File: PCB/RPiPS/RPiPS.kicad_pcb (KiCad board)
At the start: 2 copper layers, 17 parts, among them IC1 ATTINY25-P, K1 RELAI-1RT, P1 PowerIn, P2 CONN_1, P3 PiPower, Q1 NPN, SW1 SW_PUSH

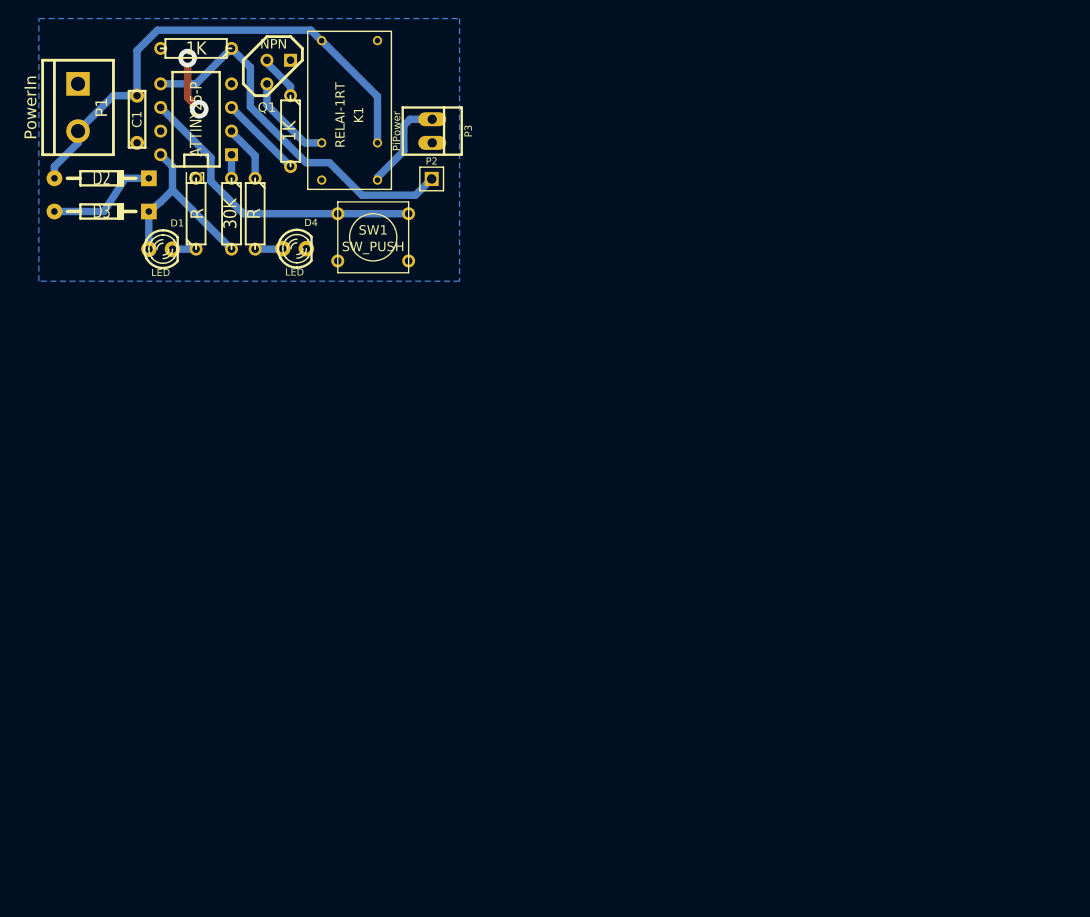
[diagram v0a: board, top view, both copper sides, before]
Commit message: Move to RPi Expansion board template
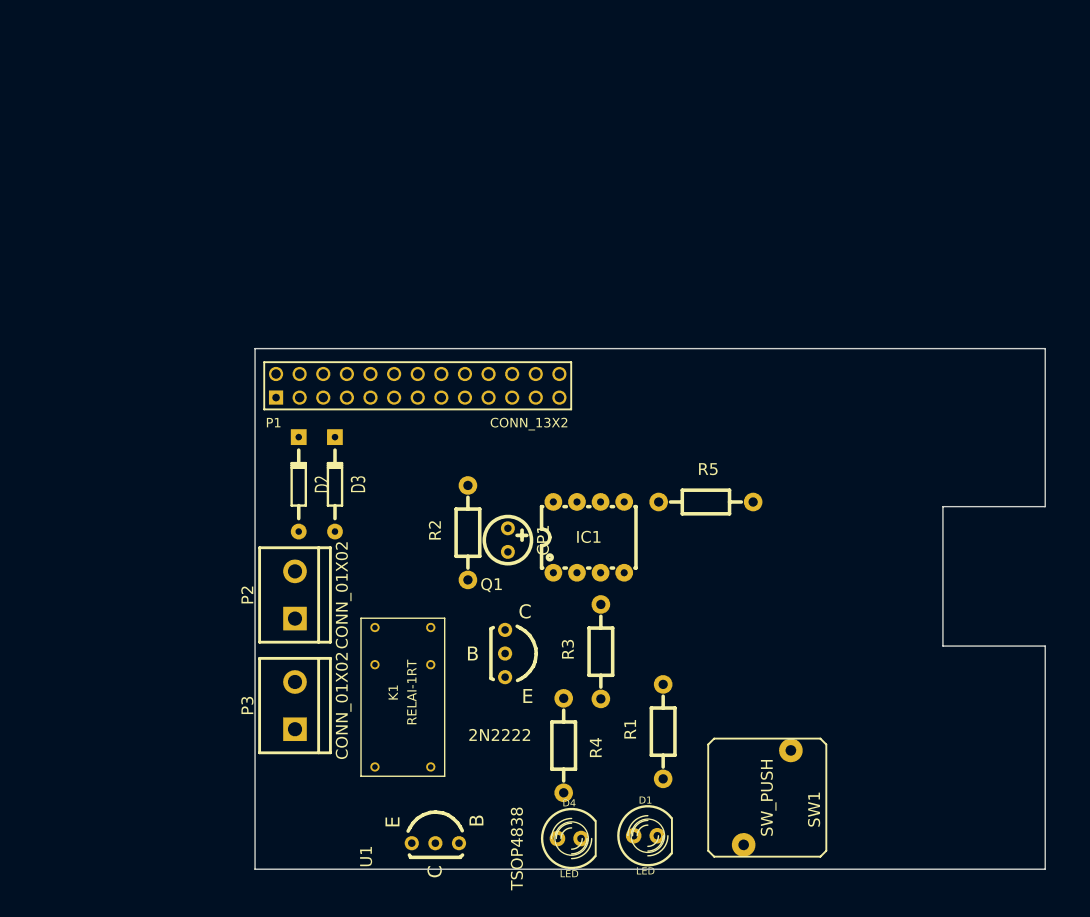
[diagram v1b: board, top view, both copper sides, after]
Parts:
- removed C1: C, Capacitors:cnp_6mm_disc
- added CP1: 100n, Capacitors_Elko_ThroughHole:Elko_vert_DM5_RM2-5, F.Cu at (170.7, 145.6)
- added U1: TSOP4838, Housings_TO-92:TO-92-Bipolar-inline-wide-ECB, F.Cu at (162.9, 178.2)
- D1, D4: footprint LEDs:LED-3MM -> LEDs:LED-5MM
- IC1: footprint Sockets_DIP:DIP-8__300 -> Power_Integrations:PDIP-8
- K1: footprint local:Relay V23040 -> relay:Relay V23040
- P1: value PowerIn -> CONN_13X2; footprint Connect:bornier2 -> pin_array_13x2
- P2: value CONN_1 -> CONN_01X02; footprint Pin_Arrays:PIN_ARRAY_1 -> Connect:bornier2
- P3: value PiPower -> CONN_01X02; footprint Connect:PINHEAD1-2 -> Connect:bornier2
- Q1: value NPN -> 2N2222; footprint Discret:TO92 -> Housings_TO-92:TO-92-Bipolar-inline-wide-CBE
- R1, R4: value R -> 100; footprint Discret:R3 -> Resistors_ThroughHole:Resistor_Horizontal_RM10mm
- R2, R3, R5: footprint Discret:R3 -> Resistors_ThroughHole:Resistor_Horizontal_RM10mm
- SW1: footprint Discret:SW_PUSH_SMALL -> Discret:SW_PUSH
- moved D1 81.9 mm to (185.5, 177.4)
- moved R1 75.0 mm to (187.4, 166.2)
- moved SW1 73.7 mm to (198.6, 173.3), turned to 270 degrees
- moved R5 73.4 mm to (192.0, 141.5), turned to 0 degrees
- moved D4 70.0 mm to (177.3, 177.7)
- moved Q1 67.1 mm to (170.4, 157.8)
- moved R4 66.1 mm to (176.7, 167.7)
- moved R3 65.2 mm to (180.7, 157.6), turned to 90 degrees
- moved P3 63.5 mm to (147.8, 163.4), turned to 90 degrees
- moved IC1 61.7 mm to (179.4, 145.3), turned to 0 degrees
- moved K1 56.4 mm to (159.4, 159.0), turned to 90 degrees
- moved P1 47.2 mm to (161.0, 129.0), turned to 0 degrees
- moved P2 47.1 mm to (147.8, 151.5), turned to 90 degrees
- moved R2 42.7 mm to (166.4, 144.8), turned to 90 degrees
- moved D2 39.2 mm to (148.2, 139.6), turned to 90 degrees
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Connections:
- D2 pad 1: +5V -> Net-(D2-Pad1)
- IC1 pad 5: Net-(IC1-Pad5) -> /GPIO17
- IC1 pad 7: (no net) -> Net-(IC1-Pad7)
- K1 pad 2: +5V -> Net-(D2-Pad1)
- K1 pad 4: (no net) -> Net-(K1-Pad4)
- K1 pad 5: +5V -> Net-(D2-Pad1)
- P1 pad 1: GND -> +3.3V
- P2 pad 1: Net-(IC1-Pad5) -> GND
- R5 pad 1: Net-(IC1-Pad5) -> /GPIO17
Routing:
- net +5V: track 53.6 -> 0.00 mm
- net Net-(IC1-Pad5): track 40.5 -> 0.00 mm
- net Net-(IC1-Pad6): track 32.9 -> 0.00 mm
- net VCC: track 20.8 -> 0.00 mm
- net Net-(D2-Pad2): track 12.1 -> 0.00 mm
- net Net-(K1-Pad6): track 10.4 -> 0.00 mm
- net Net-(K1-Pad1): track 9.84 -> 0.00 mm
- net Net-(IC1-Pad3): track 8.98 -> 0.00 mm
- net Net-(IC1-Pad2): track 6.13 -> 0.00 mm
- net GND: track 6.02 -> 0.00 mm, vias 2 -> 0
- net Net-(Q1-Pad2): track 4.86 -> 0.00 mm
- net Net-(D4-Pad1): track 2.99 -> 0.00 mm
- net Net-(IC1-Pad1): track 2.54 -> 0.00 mm
- net Net-(D1-Pad2): track 2.54 -> 0.00 mm
- removed copper zone on B.Cu, net GND
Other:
- board outline added: 85 x 56 mm
- net class Default: clearance 0.254 -> 0.2; trace_width 0.254 -> 0.2; via_dia 0.889 -> 0.9; via_drill 0.635 -> 0.6
- net class Lycée removed
- net class Power added: clearance 0.2, trace_width 0.5, via_dia 1, via_drill 0.7
- rule trace_clearance: 0.254 -> 0.2
- rule trace_min: 0.254 -> 0.1524
- rule via_min_drill: 0.508 -> 0.5
- rule via_min_size: 0.889 -> 0.8
- board text added: "1/8" JACK OK WITH STD HEADERS !NO TH ABOVE!"
- board text added: "DOUBLE USB CUTOUT FOR ALL BOARDS"
- board text added: "RASPBERRY-PI ADDON BOARD VIEW FROM TOP NOTE: P1 SHOULD BE FITTED ON THE REVERSE OF THE BOARD"
- board text added: "RCA REMOVE WITH STD HEADERS !NO TH ABOVE!"
- board text added: "RJ45 CUTOUT FOR STD HEADERS !NO TH ABOVE!"

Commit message: add IR receiver pcb routing fabrication files
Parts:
- P1: footprint pin_array_13x2 -> Pin_Arrays:pin_array_2x13
- Q1: value 2N2222 -> PN2222A; footprint Housings_TO-92:TO-92-Bipolar-inline-wide-CBE -> Discret:TO92-123
- U1: footprint Housings_TO-92:TO-92-Bipolar-inline-wide-ECB -> IR:TSOP4838
- moved U1 38.6 mm to (201.4, 175.9), turned to 0 degrees
- moved R5 13.9 mm to (178.6, 145.2), turned to 270 degrees
- moved R3 10.6 mm to (171.0, 153.4), turned to 0 degrees
- moved R1 9.00 mm to (178.4, 166.4)
- moved SW1 8.25 mm to (190.4, 172.4)
- moved IC1 8.09 mm to (171.4, 144.1)
- moved R2 7.91 mm to (158.5, 144.5)
- moved CP1 7.61 mm to (163.2, 144.3)
- moved D1 7.06 mm to (178.5, 176.5)
- moved D4 5.85 mm to (171.6, 176.4)
- moved R4 4.02 mm to (172.9, 166.4)
- moved Q1 2.90 mm to (167.5, 157.9), turned to 180 degrees
- turned D3 to 270 degrees
- turned P3 to 270 degrees
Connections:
- P1 pad 14: Net-(P1-Pad14) -> GND
- P1 pad 20: Net-(P1-Pad20) -> GND
- P1 pad 25: Net-(P1-Pad25) -> GND
- P1 pad 4: Net-(P1-Pad4) -> +5V
- P1 pad 9: Net-(P1-Pad9) -> GND
- R3 pad 1: Net-(Q1-Pad2) -> Net-(Q1-Pad1)
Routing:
- net +3.3V: track 0.00 -> 109.7 mm
- net /GPIO18: track 0.00 -> 84.9 mm
- net VCC: track 0.00 -> 71.8 mm
- net Net-(IC1-Pad6): track 0.00 -> 41.1 mm
- net Net-(D2-Pad1): track 0.00 -> 36.4 mm
- net /GPIO17: track 0.00 -> 26.1 mm
- net Net-(IC1-Pad2): track 0.00 -> 14.6 mm
- net GND: track 0.00 -> 13.5 mm
- net Net-(K1-Pad6): track 0.00 -> 11.0 mm
- net Net-(IC1-Pad1): track 0.00 -> 9.78 mm
- net Net-(D4-Pad1): track 0.00 -> 7.14 mm
- net Net-(IC1-Pad3): track 0.00 -> 6.90 mm
- net Net-(D1-Pad2): track 0.00 -> 5.59 mm
- net Net-(Q1-Pad1): track 0.00 -> 4.41 mm
- net Net-(K1-Pad1): track 0.00 -> 3.90 mm
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- added copper zone on B.Cu, net GND
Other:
- board text added: "Pin"
- board text added: "Ppi"
- board text added: "boot ok"
- board text added: "power on"

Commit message: OSHW logo relay footprint
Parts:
- added SYM: Symbol_OSHW-Logo_CopperTop_07Jul2012, Footprint_Symbols:Symbol_OSHW-Logo_CopperTop, B.Cu at (222.4, 130.3)
- K1: footprint relay:Relay V23040 -> Relay_V23040
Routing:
- net GND: track 13.5 -> 0.54 mm
- net Net-(D2-Pad1): track 36.4 -> 37.7 mm
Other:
- board text added: "CC:BY-SA"
- board text added: "https://github.com/jerome-labidurie/RPiSU"

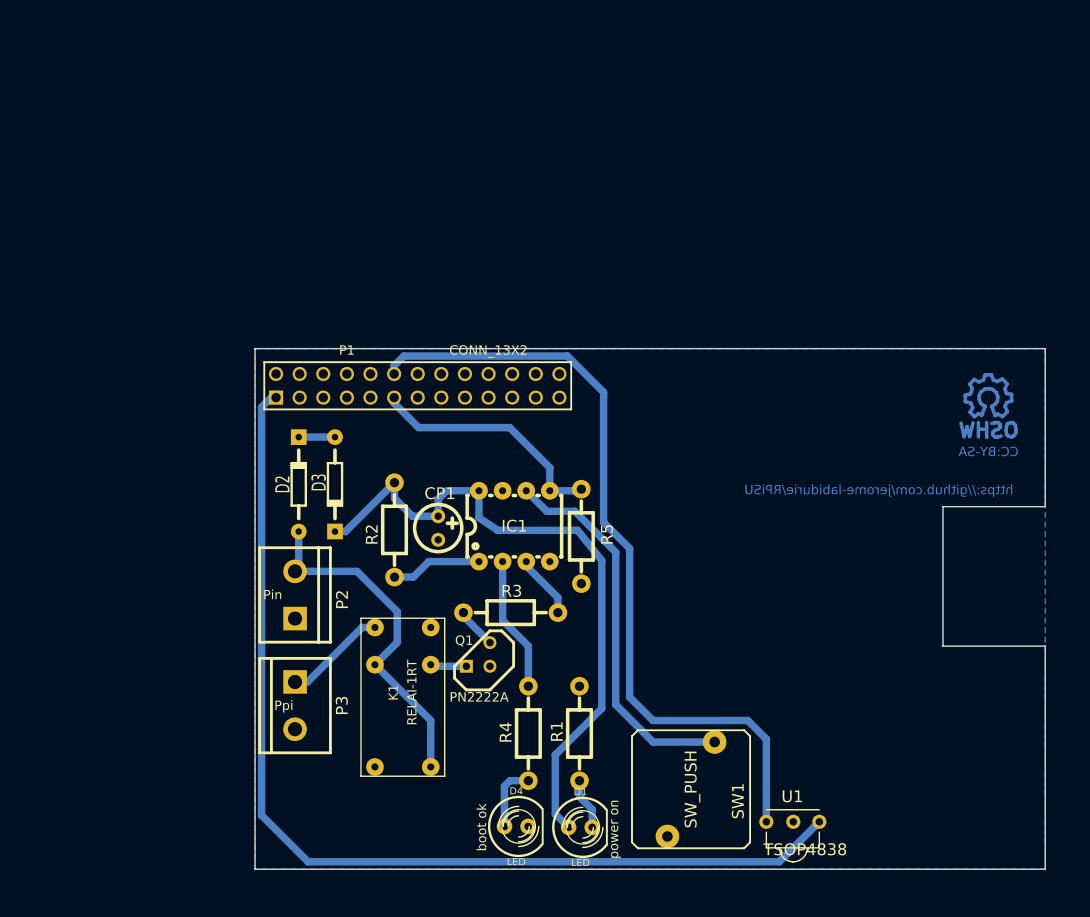
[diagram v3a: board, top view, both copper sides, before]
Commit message: remove gnd plane over Pi connectors reverse P2 (1 is +) minor Silk adjustment
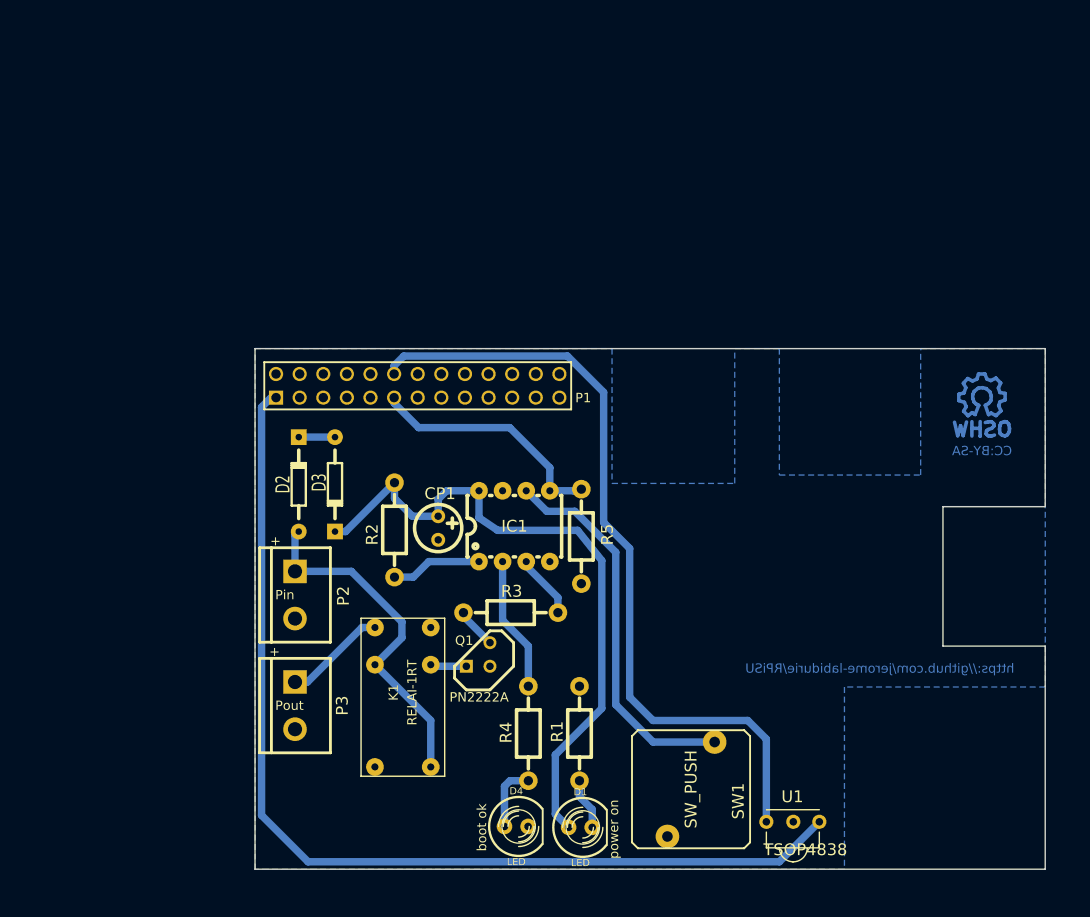
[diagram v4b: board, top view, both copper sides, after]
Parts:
- moved SYM 0.71 mm to (221.7, 130.2)
- turned P2 to 270 degrees
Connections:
- P2 pad 1: GND -> Net-(D2-Pad1)
- P2 pad 2: Net-(D2-Pad1) -> GND
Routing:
- net Net-(D2-Pad1): track 37.7 -> 38.4 mm
- net GND: track 0.54 -> 0.00 mm
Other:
- board text added: "+"
- board text added: "Pout"
- board text removed: "Ppi"
